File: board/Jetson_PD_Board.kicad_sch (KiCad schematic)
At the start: 22 parts, among them J1 USB4081-03-A, Q1 NTTFS5C673NLTAG, Q2 NTTFS5C673NLTAG, Q3 NTTFS5C673NLTAG, U1 APK43070DKZ-13-FA01

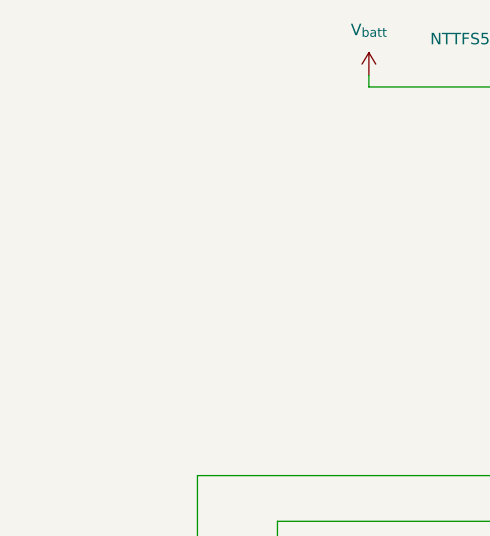
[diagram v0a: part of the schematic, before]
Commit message: Added Power Connector
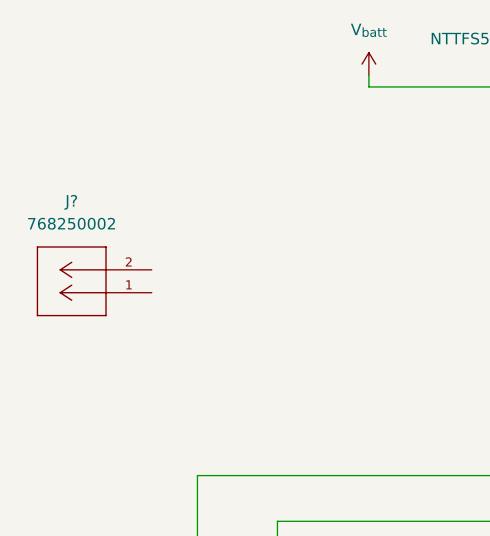
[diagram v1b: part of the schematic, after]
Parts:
- added J?: 768250002, PD_Hardware_Footprints:CONN_SD-76825-0100_02_MOL, symbol PowerManagementBoard:768250002
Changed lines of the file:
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@@
+	)
+	(symbol
+		(lib_id "PowerManagementBoard:768250002")
+		(at 38.1 72.39 180)
+		(unit 1)
+		(exclude_from_sim no)
+		(in_bom yes)
+		(on_board yes)
+		(dnp no)
+		(fields_autoplaced yes)
+		(property "Reference" "J?"
+			(at 29.21 62.23 0)
+			(effects
+				(font
+					(size 1.27 1.27)
+				)
+			)
+		)
+		(property "Value" "768250002"
+			(at 29.21 64.77 0)
+			(effects
+				(font
+					(size 1.27 1.27)
+				)
+			)
+		)
+		(property "Footprint" "PD_Hardware_Footprints:CONN_SD-76825-0100_02_MOL"
+			(at 38.1 72.39 0)
+			(effects
+				(font
+					(size 1.27 1.27)
+				)
+				(justify bottom)
+				(hide yes)
+			)
+		)
+		(property "Datasheet" "https://mm.digikey.com/Volume0/opasdata/d220001/medias/docus/1100/Mega-Fit_Power_Conn.pdf"
+			(at 38.1 72.39 0)
+			(effects
+				(font
+					(size 1.27 1.27)
+				)
+				(hide yes)
+			)
+		)
+		(property "Description" ""
+			(at 38.1 72.39 0)
+			(effects
+				(font
+					(size 1.27 1.27)
+				)
+				(hide yes)
+			)
+		)
+		(property "MFR_NAME" "Molex Connector Corporation"
+			(at 38.1 72.39 0)
+			(effects
+				(font
+					(size 1.27 1.27)
+				)
+				(justify bottom)
+				(hide yes)
+			)
+		)
+		(property "MANUFACTURER_PART_NUMBER" "768250002"
+			(at 38.1 72.39 0)
+			(effects
+				(font
+					(size 1.27 1.27)
+				)
+				(justify bottom)
+				(hide yes)
+			)
+		)
+		(pin "2"
+		)
+		(pin "1"
+		)
+		(instances
+			(project "Jetson_PD_Board"
+				(path "/fbd9c71c-f200-4aab-a303-9f269bc9de13"
+					(reference "J?")
+					(unit 1)
+				)
+			)
+		)
 	)
 	(symbol

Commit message: finished schematic maybe
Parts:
- added C10: 100nF, symbol Device:C
- added C9: 4.7uF, symbol Device:C
- added U2: USBLC6-2SC6, Package_TO_SOT_SMD:SOT-23-6, symbol Power_Protection:USBLC6-2SC6
- gave numbers to parts that had none: 1
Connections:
- net GND: no longer C1.2, C2.2, Q2.3 (S), U1.14 (PGND)
- net V_{batt}: now also J2.2, Q1.1 (D)
- net V_{out}: now also C10.1, C9.1, U2.5 (VBUS)
- net at Q3.3 (S): now also C2.1, L1.2, R5.1, U1.24 (CSP); no longer Q1.1 (D)
- net P_{GND}: now reaches J2.1
- net P_{GND}: now also C1.2, C2.2, J1.A1 (GND), J1.A12 (GND), J1.B1 (GND), J1.B12 (GND), Q2.3 (S), U1.14 (PGND), C10.2, C9.2, U2.2 (GND)
- net DN: no longer names the net of U1.4 (DN)
- net DN: now also U2.3 (I/O2); no longer J1.B7 (DN2)
- net DP: no longer names the net of U1.5 (DP)
- net DP: now also U2.1 (I/O1); no longer J1.B6 (DP2)
- new net: J1.B7 (DN2), U2.4 (I/O2)
- new net: J1.B6 (DP2), U2.6 (I/O1)
- no-connect marks 1 -> 3
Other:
- moved on the sheet: J1, J2, Q3

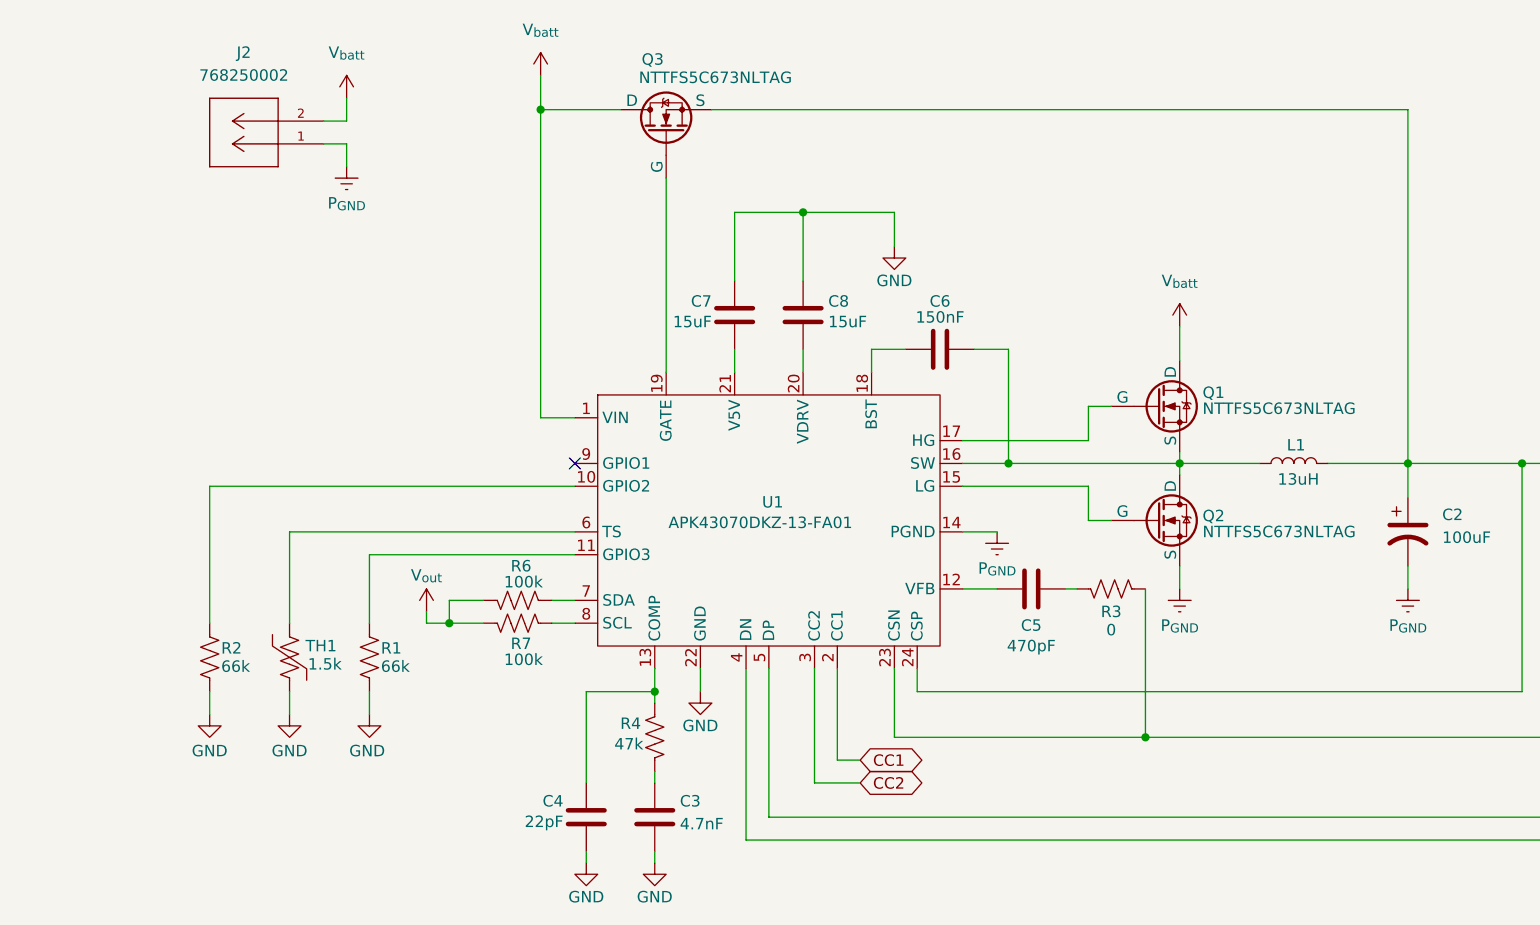
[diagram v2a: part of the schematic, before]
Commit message: Added all footprints and 3D models
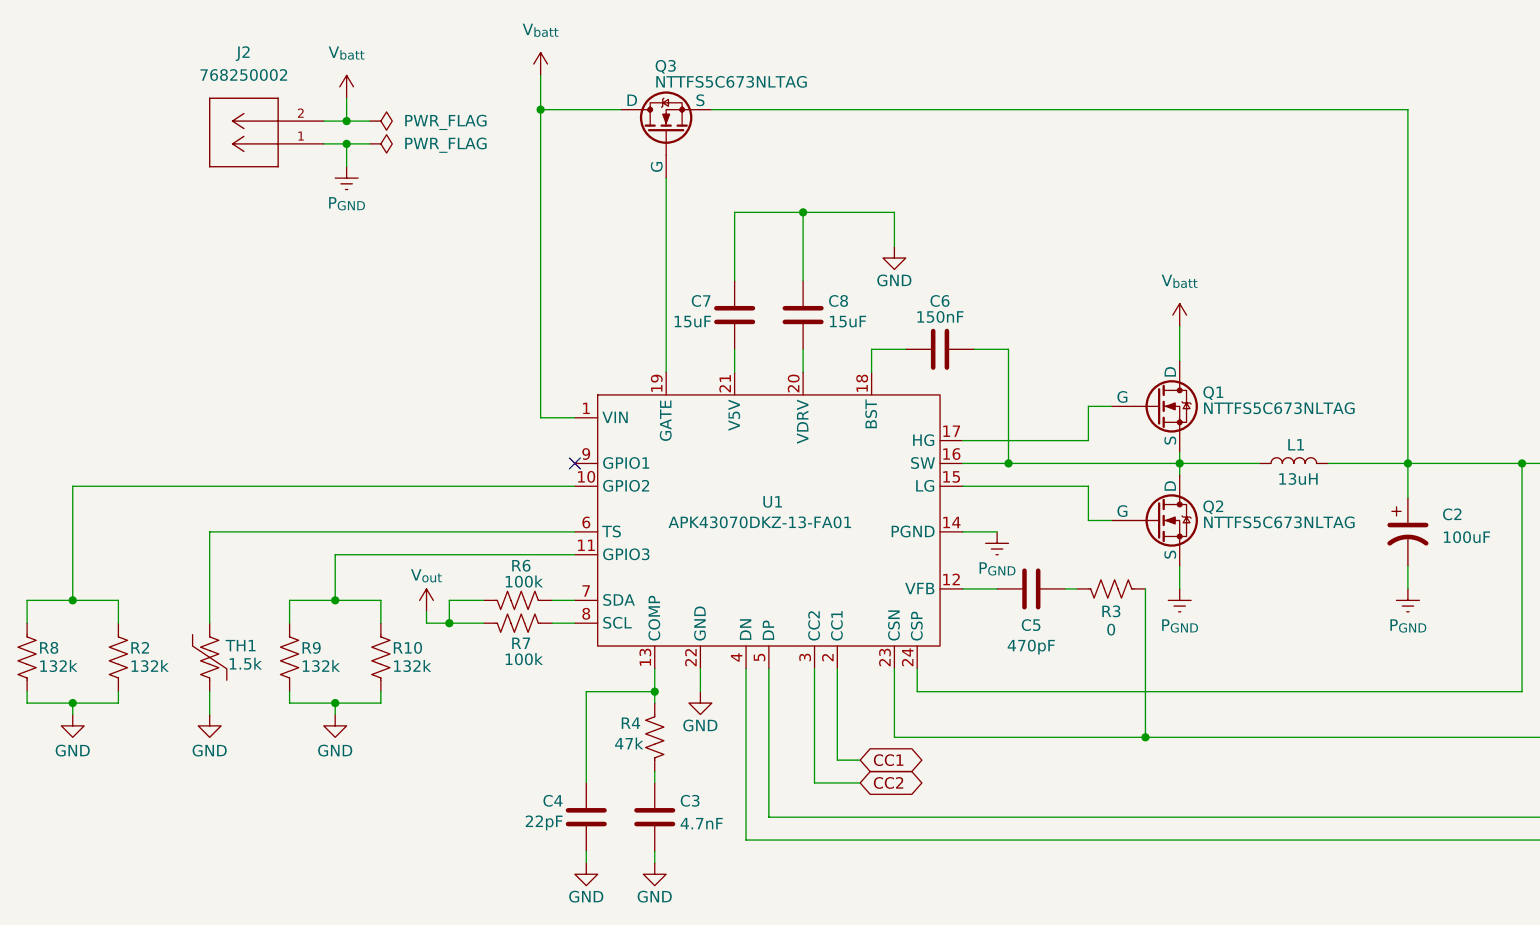
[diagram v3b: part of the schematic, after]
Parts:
- removed R1: 66k, symbol Device:R_US
- added R10, R8, R9: 132k, Resistor_SMD:R_0603_1608Metric_Pad0.98x0.95mm_HandSolder, symbol Device:R_US
- C10, C3, C4, C5, C6, C7, C8, C9: footprint (none) -> Capacitor_SMD:C_0603_1608Metric_Pad1.08x0.95mm_HandSolder
- C2: footprint (none) -> PD_Hardware_Footprints:CAP_RHA&slash_HS_8X8P7_NCH-M
- J1: footprint CONN24_USB4081_GCT -> PD_Hardware_Footprints:CONN24_USB4081_GCT
- L1: footprint (none) -> PD_Hardware_Footprints:WE-PDF_1064
- Q1, Q2, Q3: footprint (none) -> PD_Hardware_Footprints:TRANS_NVTFS5116PLTAG
- R2: value 66k -> 132k; footprint (none) -> Resistor_SMD:R_0603_1608Metric_Pad0.98x0.95mm_HandSolder
- R3, R4, R6, R7, TH1: footprint (none) -> Resistor_SMD:R_0603_1608Metric_Pad0.98x0.95mm_HandSolder
- R5: footprint (none) -> Resistor_SMD:R_2512_6332Metric_Pad1.40x3.35mm_HandSolder
- U1: footprint (none) -> PD_Hardware_Footprints:IC_AP33771DKZ-13
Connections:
- net GND: now also R10.2, R8.2, R9.2
- net at R2.1, U1.10 (GPIO2): now also R8.1
- net at U1.11 (GPIO3): now also R10.1, R9.1
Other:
- moved on the sheet: TH1

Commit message: Fixed ERC errors
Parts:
- L1: value 13uH -> L; Part Number 7447798131 -> (none)
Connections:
- net P_{GND} is gone; now on net GND: C1.2, C10.2, C2.2, C9.2, J1.A1 (GND), J1.A12 (GND), J1.B1 (GND), J1.B12 (GND), J2.1, Q2.3 (S), U1.14 (PGND), U2.2 (GND)
- no-connect marks 3 -> 13
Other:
- moved on the sheet: Q1

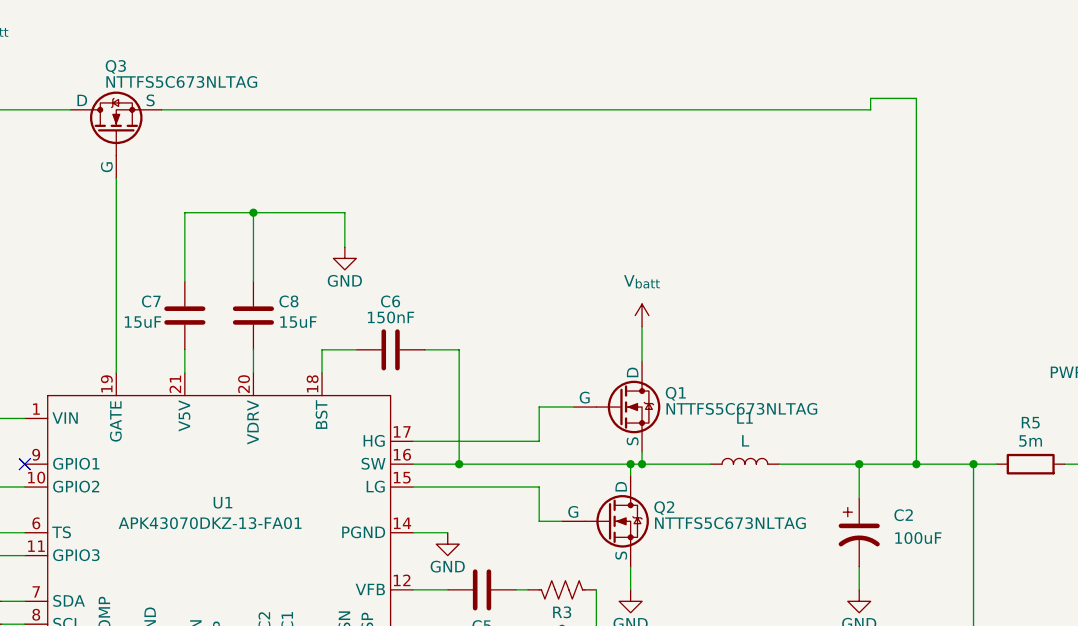
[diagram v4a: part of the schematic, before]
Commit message: Fixed 3d all 3D model file paths
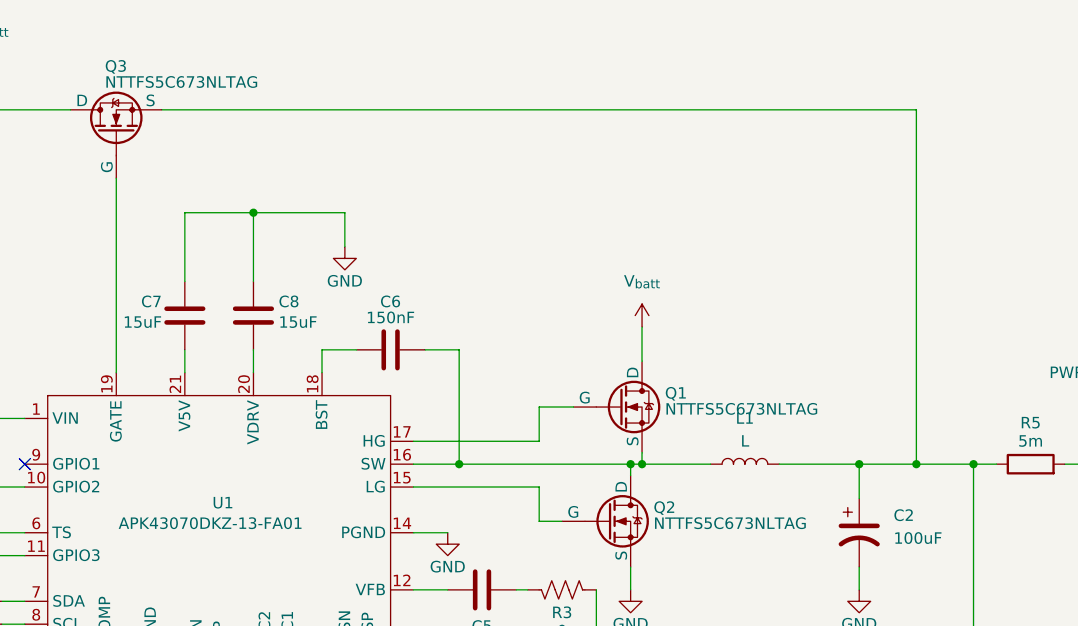
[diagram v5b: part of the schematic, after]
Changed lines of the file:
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@@
-	(wire
-		(pts
-			(xy 177.8 49.53) (xy 182.88 49.53)
-		)
-		(stroke
-			(width 0)
-			(type default)
-		)
-	)
 	(wire
 		(pts
@@
 	(wire
 		(pts
-			(xy 177.8 49.53) (xy 177.8 50.8)
-		)
-		(stroke
-			(width 0)
-			(type default)
-		)
-	)
-	(wire
-		(pts
 			(xy 80.01 50.8) (xy 88.9 50.8)
 		)
@@
 	(wire
 		(pts
-			(xy 177.8 50.8) (xy 99.06 50.8)
+			(xy 99.06 50.8) (xy 182.88 50.8)
 		)
 		(stroke
@@
 	(wire
 		(pts
-			(xy 182.88 49.53) (xy 182.88 90.17)
-		)
-		(stroke
+			(xy 182.88 50.8) (xy 182.88 90.17)
+		)
+		(stroke

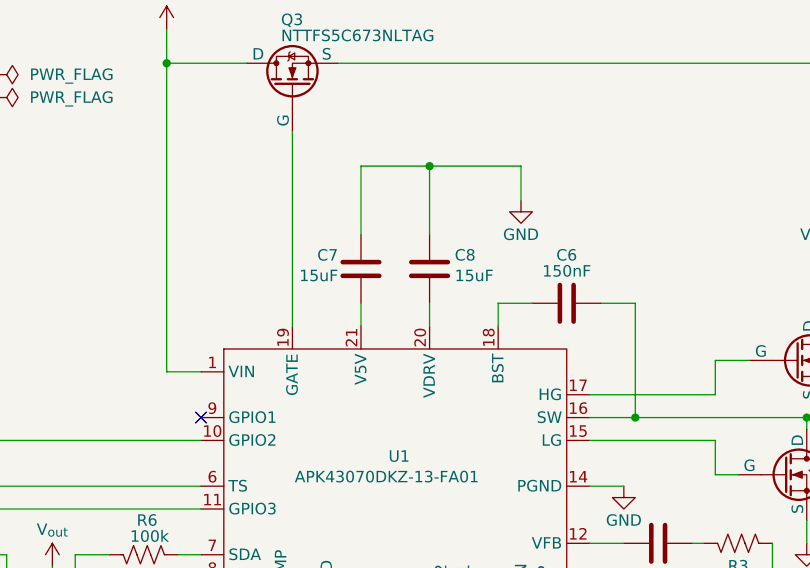
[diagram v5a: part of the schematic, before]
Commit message: Fixed missing pad gnd
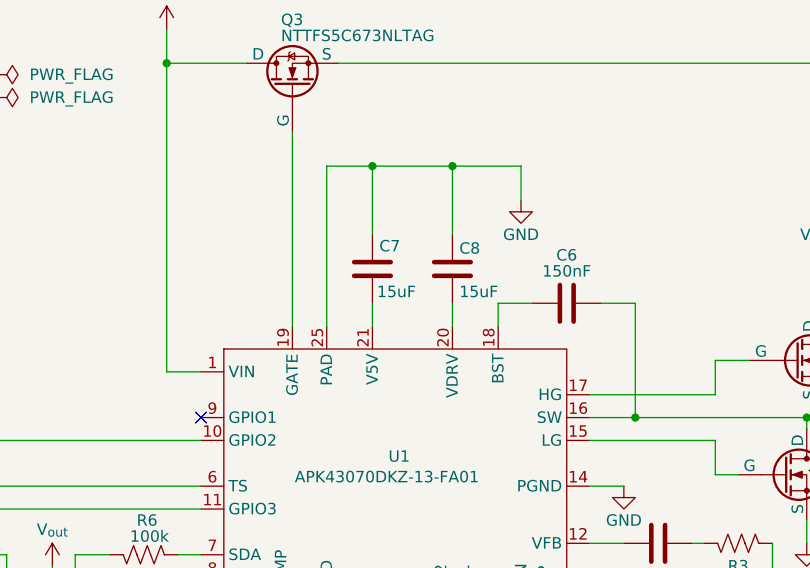
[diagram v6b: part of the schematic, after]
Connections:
- net GND: now also U1.25 (PAD)
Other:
- moved on the sheet: C7, C8
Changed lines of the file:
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@@
 	)
 	(junction
-		(at 109.22 62.23)
-		(diameter 0)
-		(color 0 0 0 0)
-	)
-	(junction
 		(at 242.57 77.47)
 		(diameter 0)
@@
 	)
 	(junction
+		(at 111.76 62.23)
+		(diameter 0)
+		(color 0 0 0 0)
+	)
+	(junction
 		(at 201.93 90.17)
 		(diameter 0)
@@
 	)
 	(junction
+		(at 102.87 62.23)
+		(diameter 0)
+		(color 0 0 0 0)
+	)
+	(junction
 		(at 152.4 90.17)
 		(diameter 0)
@@
 	(wire
 		(pts
-			(xy 109.22 77.47) (xy 109.22 80.01)
+			(xy 111.76 77.47) (xy 111.76 80.01)
 		)
 		(stroke
@@
 	(wire
 		(pts
-			(xy 109.22 62.23) (xy 101.6 62.23)
+			(xy 102.87 62.23) (xy 111.76 62.23)
 		)
 		(stroke
@@
 	(wire
 		(pts
+			(xy 97.79 62.23) (xy 102.87 62.23)
+		)
+		(stroke
+			(width 0)
+			(type default)
+		)
+	)
+	(wire
+		(pts
 			(xy 92.71 125.73) (xy 92.71 124.46)
 		)
@@
 	(wire
 		(pts
-			(xy 119.38 62.23) (xy 109.22 62.23)
+			(xy 119.38 62.23) (xy 111.76 62.23)
 		)
 		(stroke
@@
 	(wire
 		(pts
-			(xy 101.6 77.47) (xy 101.6 80.01)
+			(xy 102.87 77.47) (xy 102.87 80.01)
 		)
 		(stroke
@@
 	(wire
 		(pts
-			(xy 101.6 62.23) (xy 101.6 69.85)
+			(xy 102.87 62.23) (xy 102.87 69.85)
 		)
 		(stroke
@@
 	(wire
 		(pts
-			(xy 109.22 62.23) (xy 109.22 69.85)
+			(xy 111.76 62.23) (xy 111.76 69.85)
 		)
 		(stroke
@@
 	(wire
 		(pts
+			(xy 97.79 80.01) (xy 97.79 62.23)
+		)
+		(stroke
+			(width 0)
+			(type default)
+		)
+	)
+	(wire
+		(pts
 			(xy 212.09 90.17) (xy 212.09 93.98)
 		)
@@
 	(symbol
 		(lib_id "Device:C")
-		(at 101.6 73.66 0)
-		(mirror x)
+		(at 102.87 73.66 180)
 		(unit 1)
 		(exclude_from_sim no)
@@
 		(dnp no)
 		(property "Reference" "C7"
-			(at 99.06 72.136 0)
+			(at 103.632 71.12 0)
 			(effects
 				(font
@@
 		)
 		(property "Value" "15uF"
-			(at 99.06 74.422 0)
+			(at 103.378 76.2 0)
 			(effects
 				(font
@@
 		)
 		(property "Footprint" "Capacitor_SMD:C_0603_1608Metric_Pad1.08x0.95mm_HandSolder"
-			(at 102.5652 69.85 0)
+			(at 101.9048 69.85 0)
 			(effects
 				(font
@@
 		)
 		(property "Datasheet" "https://www.digikey.com/en/products/detail/samsung-electro-mechanics/CL10X106MO8NRNC/5961253"
-			(at 101.6 73.66 0)
+			(at 102.87 73.66 0)
 			(effects
 				(font
@@
 		)
 		(property "Description" "Unpolarized capacitor"
-			(at 101.6 73.66 0)
+			(at 102.87 73.66 0)
 			(effects
 				(font
@@
 		(pin "12"
 		)
+		(pin "25"
+		)
 		(instances
 			(project ""
@@
 	(symbol
 		(lib_id "Device:C")
-		(at 109.22 73.66 0)
+		(at 111.76 73.66 0)
 		(unit 1)
 		(exclude_from_sim no)
@@
 		(dnp no)
 		(property "Reference" "C8"
-			(at 112.014 72.136 0)
+			(at 112.522 71.374 0)
 			(effects
 				(font
@@
 		)
 		(property "Value" "15uF"
-			(at 112.014 74.422 0)
+			(at 112.522 76.2 0)
 			(effects
 				(font
@@
 		)
 		(property "Footprint" "Capacitor_SMD:C_0603_1608Metric_Pad1.08x0.95mm_HandSolder"
-			(at 110.1852 77.47 0)
+			(at 112.7252 77.47 0)
 			(effects
 				(font
@@
 		)
 		(property "Datasheet" "https://www.digikey.com/en/products/detail/samsung-electro-mechanics/CL10X106MO8NRNC/5961253"
-			(at 109.22 73.66 0)
+			(at 111.76 73.66 0)
 			(effects
 				(font
@@
 		)
 		(property "Description" "Unpolarized capacitor"
-			(at 109.22 73.66 0)
+			(at 111.76 73.66 0)
 			(effects
 				(font

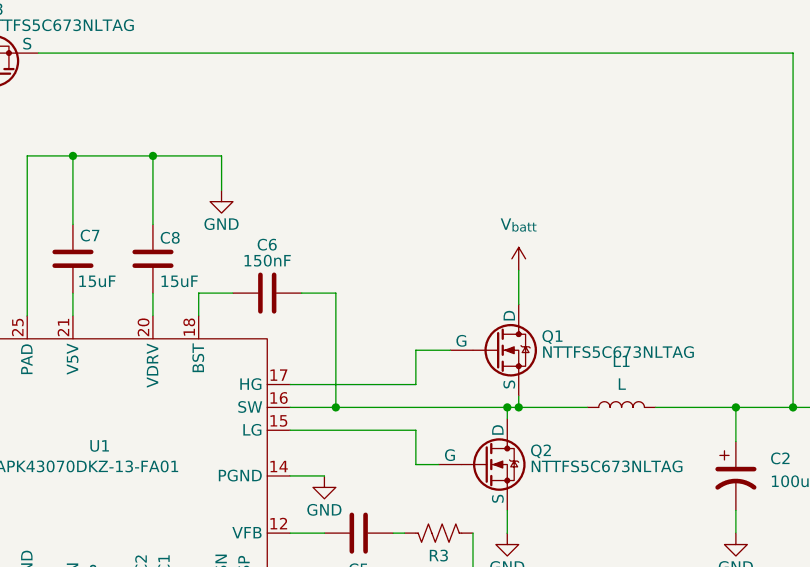
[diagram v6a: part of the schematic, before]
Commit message: Labeled switching node
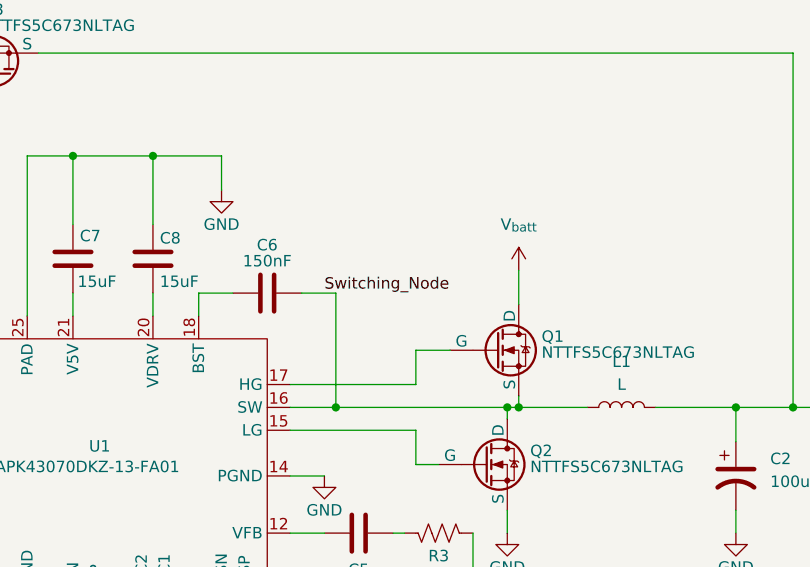
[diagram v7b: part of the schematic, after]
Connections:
- net Switching_Node: now reaches C6.1, L1.1, Q1.3 (S), Q2.1 (D), U1.16 (SW)
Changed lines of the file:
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@@
+		)
+	)
+	(label "Switching_Node"
+		(at 130.81 77.47 0)
+		(effects
+			(font
+				(size 1.27 1.27)
+			)
+			(justify left bottom)
 		)
 	)
